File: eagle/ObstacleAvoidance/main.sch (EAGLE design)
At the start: 19 parts, among them IC1 L293D, X1 JST-XH-02-PIN-LONG-PAD, X2 JST-XH-02-PIN-LONG-PAD, X3 JST-XH-04-PIN-LONG-PAD

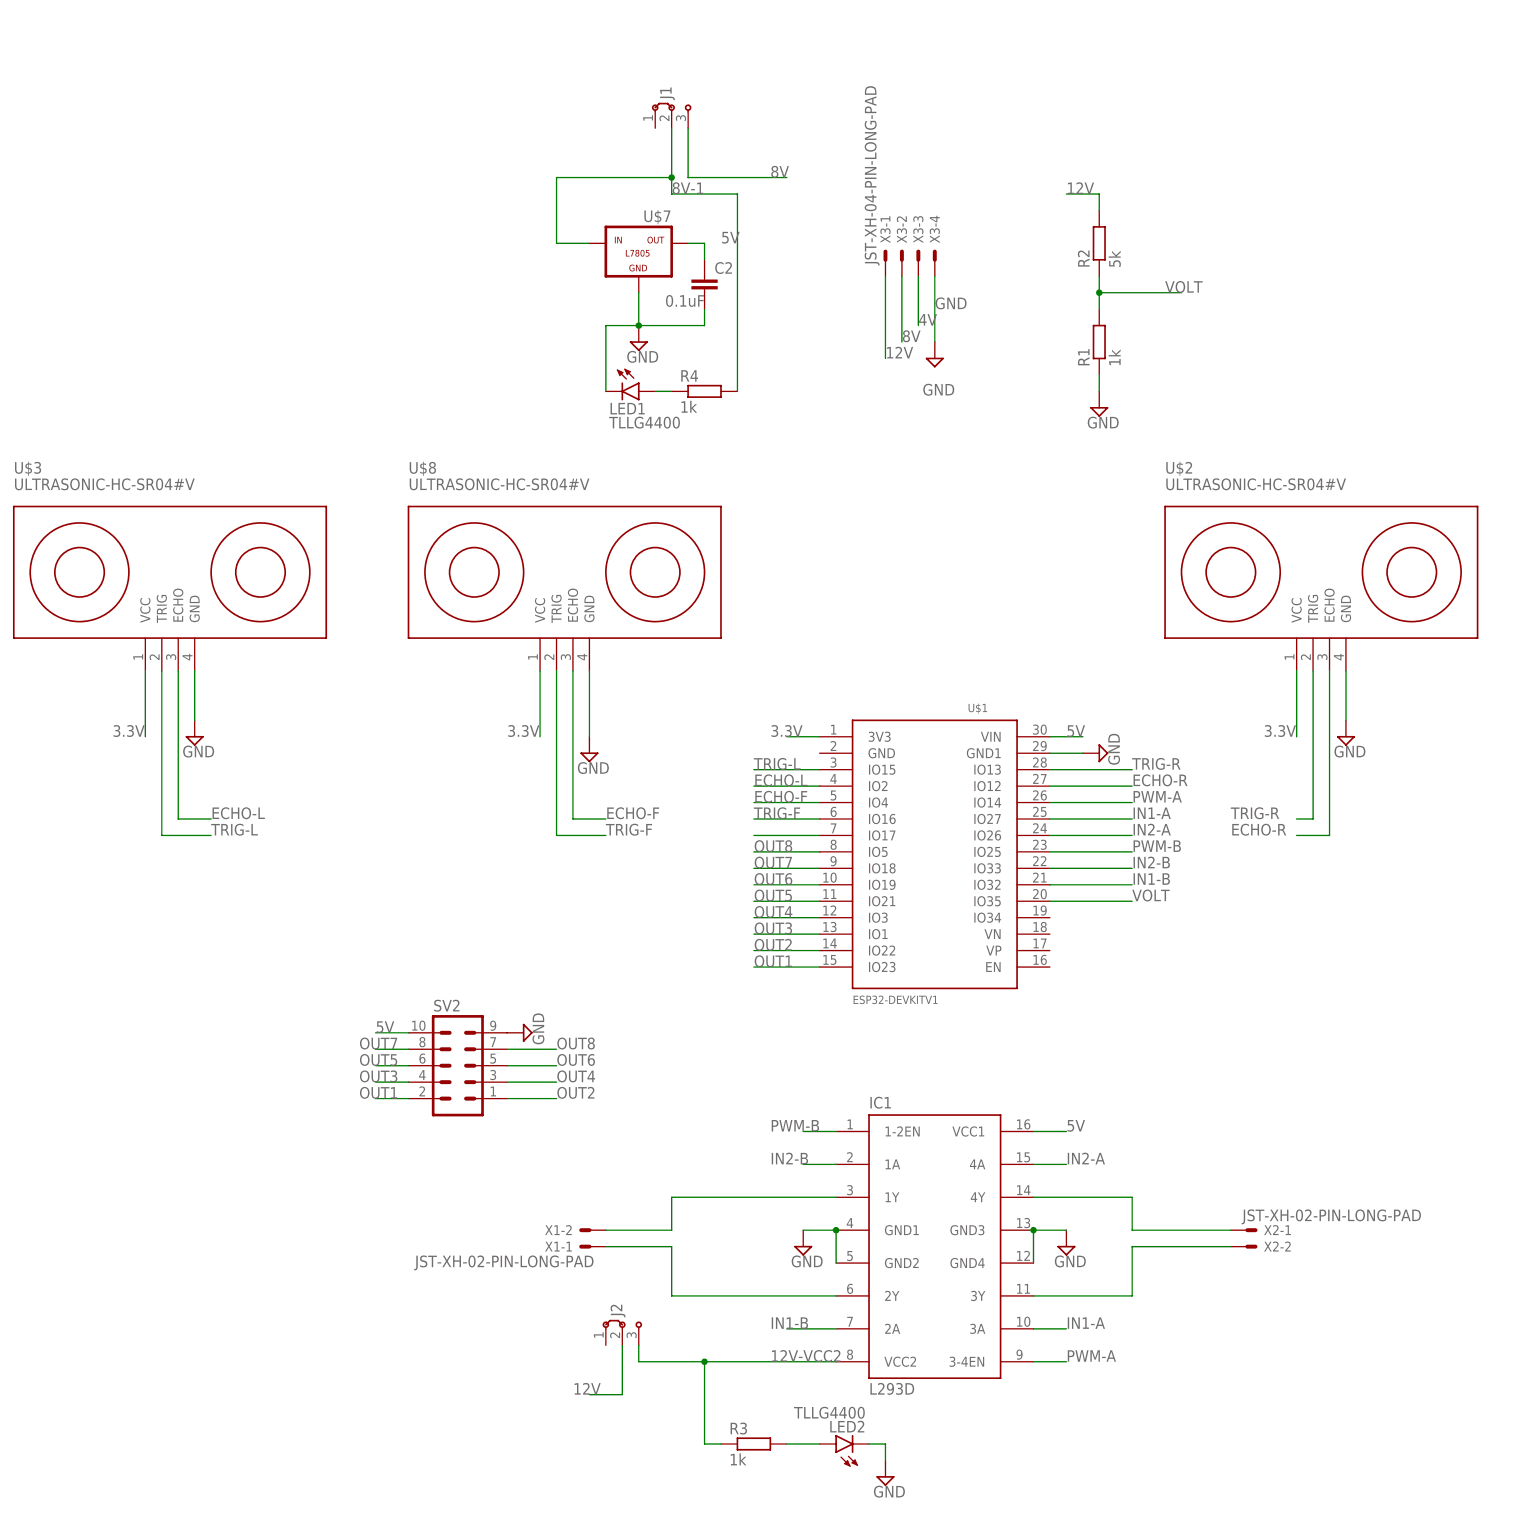
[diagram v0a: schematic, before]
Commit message: Feat: New PCB routing
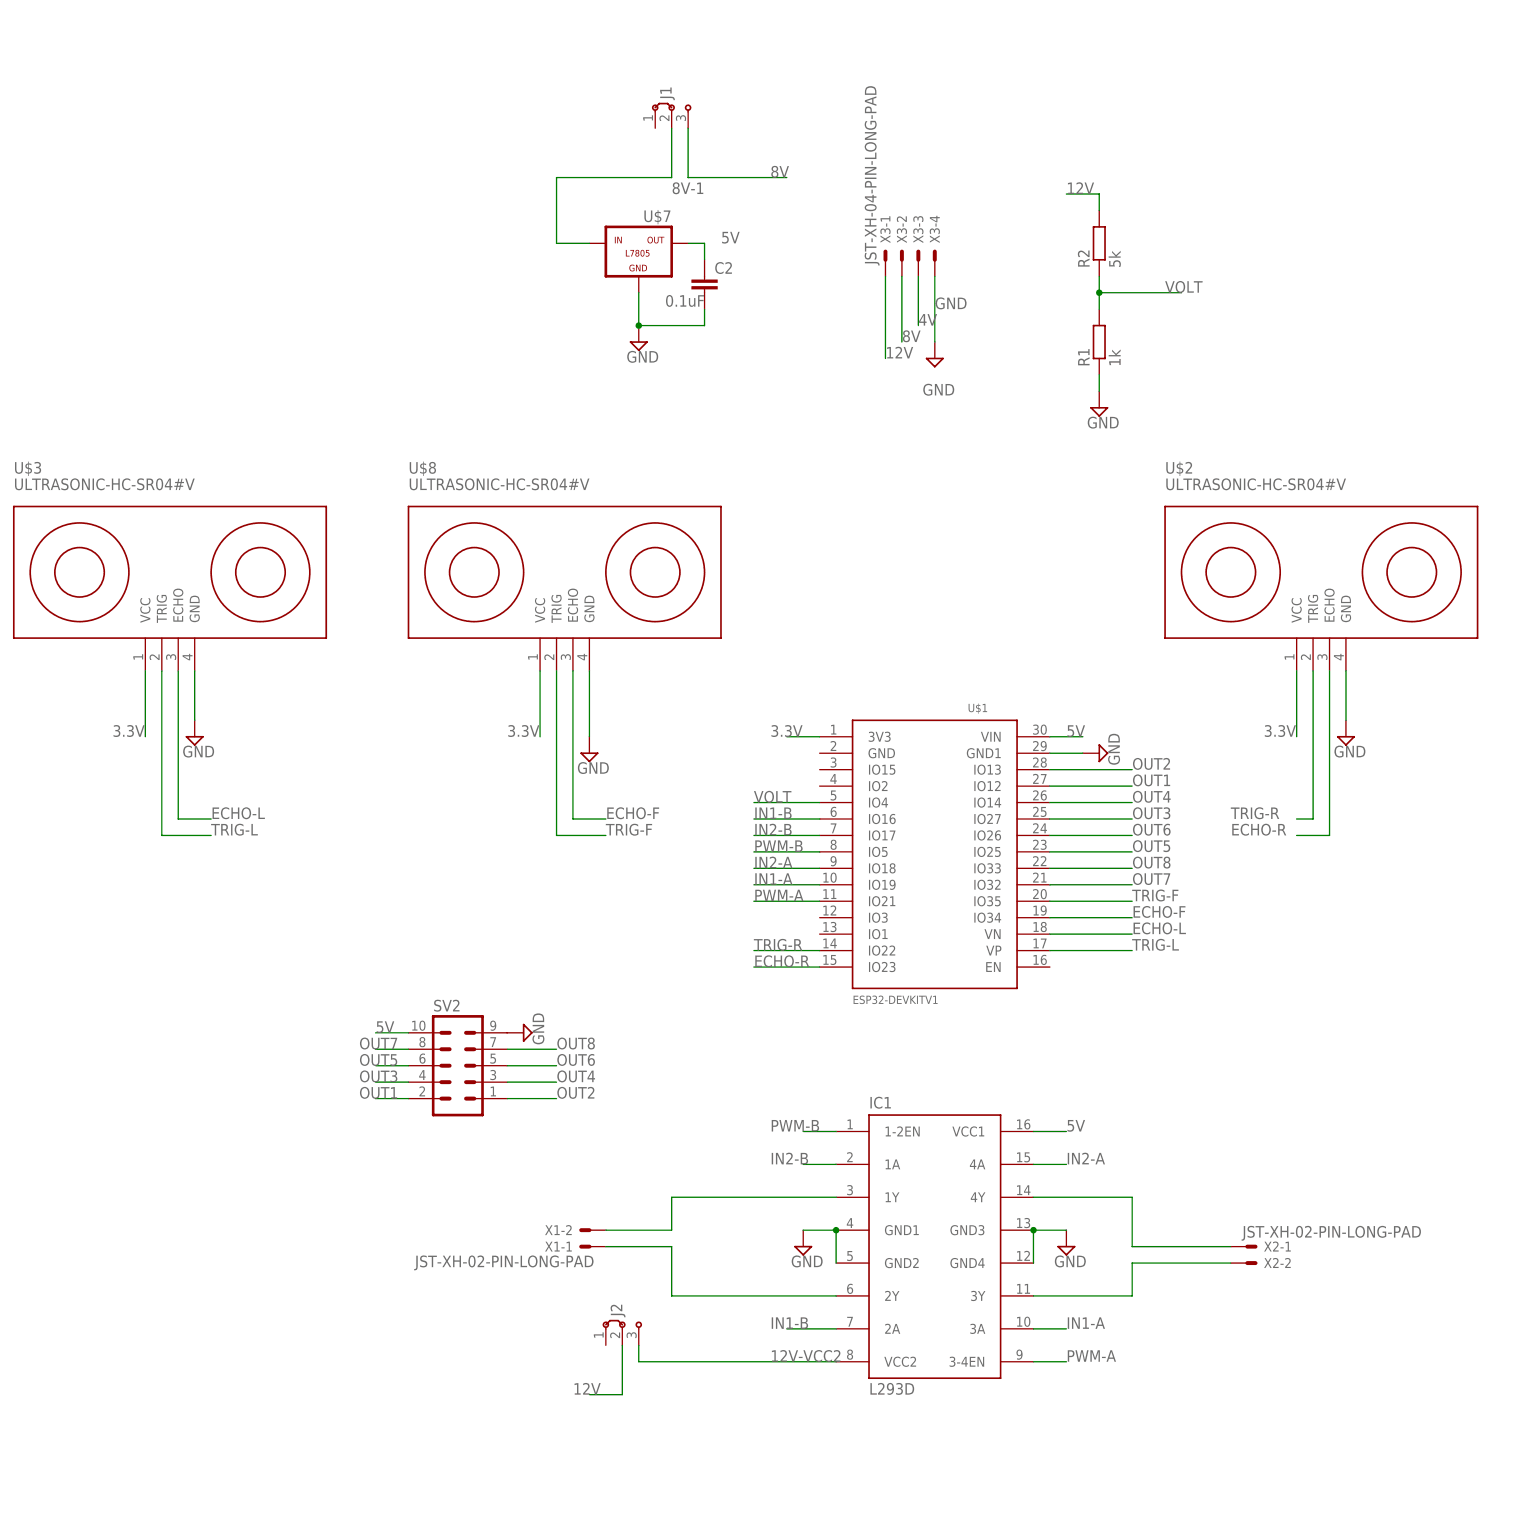
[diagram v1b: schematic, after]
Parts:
- removed LED1, LED2: TLLG4400, led:TLLG4400
- removed R3, R4: 1k, rcl:R-EU_0207/10
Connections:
- removed net N$15: U$1.IO17
- removed net N$5: LED1.A, R4.1
- removed net N$9: LED2.A, R3.2
- net 12V-VCC2: no longer R3.1
- net 8V-1: no longer R4.2
- net ECHO-F: now also U$1.IO34; no longer U$1.IO4
- net ECHO-L: now also U$1.VN; no longer U$1.IO2
- net ECHO-R: now also U$1.IO23; no longer U$1.IO12
- net GND: no longer LED1.C, LED2.C
- net IN1-A: now also U$1.IO19; no longer U$1.IO27
- net IN1-B: now also U$1.IO16; no longer U$1.IO32
- net IN2-A: now also U$1.IO18; no longer U$1.IO26
- net IN2-B: now also U$1.IO17; no longer U$1.IO33
- net OUT1: now also U$1.IO12; no longer U$1.IO23
- net OUT2: now also U$1.IO13; no longer U$1.IO22
- net OUT3: now also U$1.IO27; no longer U$1.IO1
- net OUT4: now also U$1.IO14; no longer U$1.IO3
- net OUT5: now also U$1.IO25; no longer U$1.IO21
- net OUT6: now also U$1.IO26; no longer U$1.IO19
- net OUT7: now also U$1.IO32; no longer U$1.IO18
- net OUT8: now also U$1.IO33; no longer U$1.IO5
- net PWM-A: now also U$1.IO21; no longer U$1.IO14
- net PWM-B: now also U$1.IO5; no longer U$1.IO25
- net TRIG-F: now also U$1.IO35; no longer U$1.IO16
- net TRIG-L: now also U$1.VP; no longer U$1.IO15
- net TRIG-R: now also U$1.IO22; no longer U$1.IO13
- net VOLT: now also U$1.IO4; no longer U$1.IO35
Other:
- moved on the sheet: X2-1, X2-2

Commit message: Feat: Deleted buttons
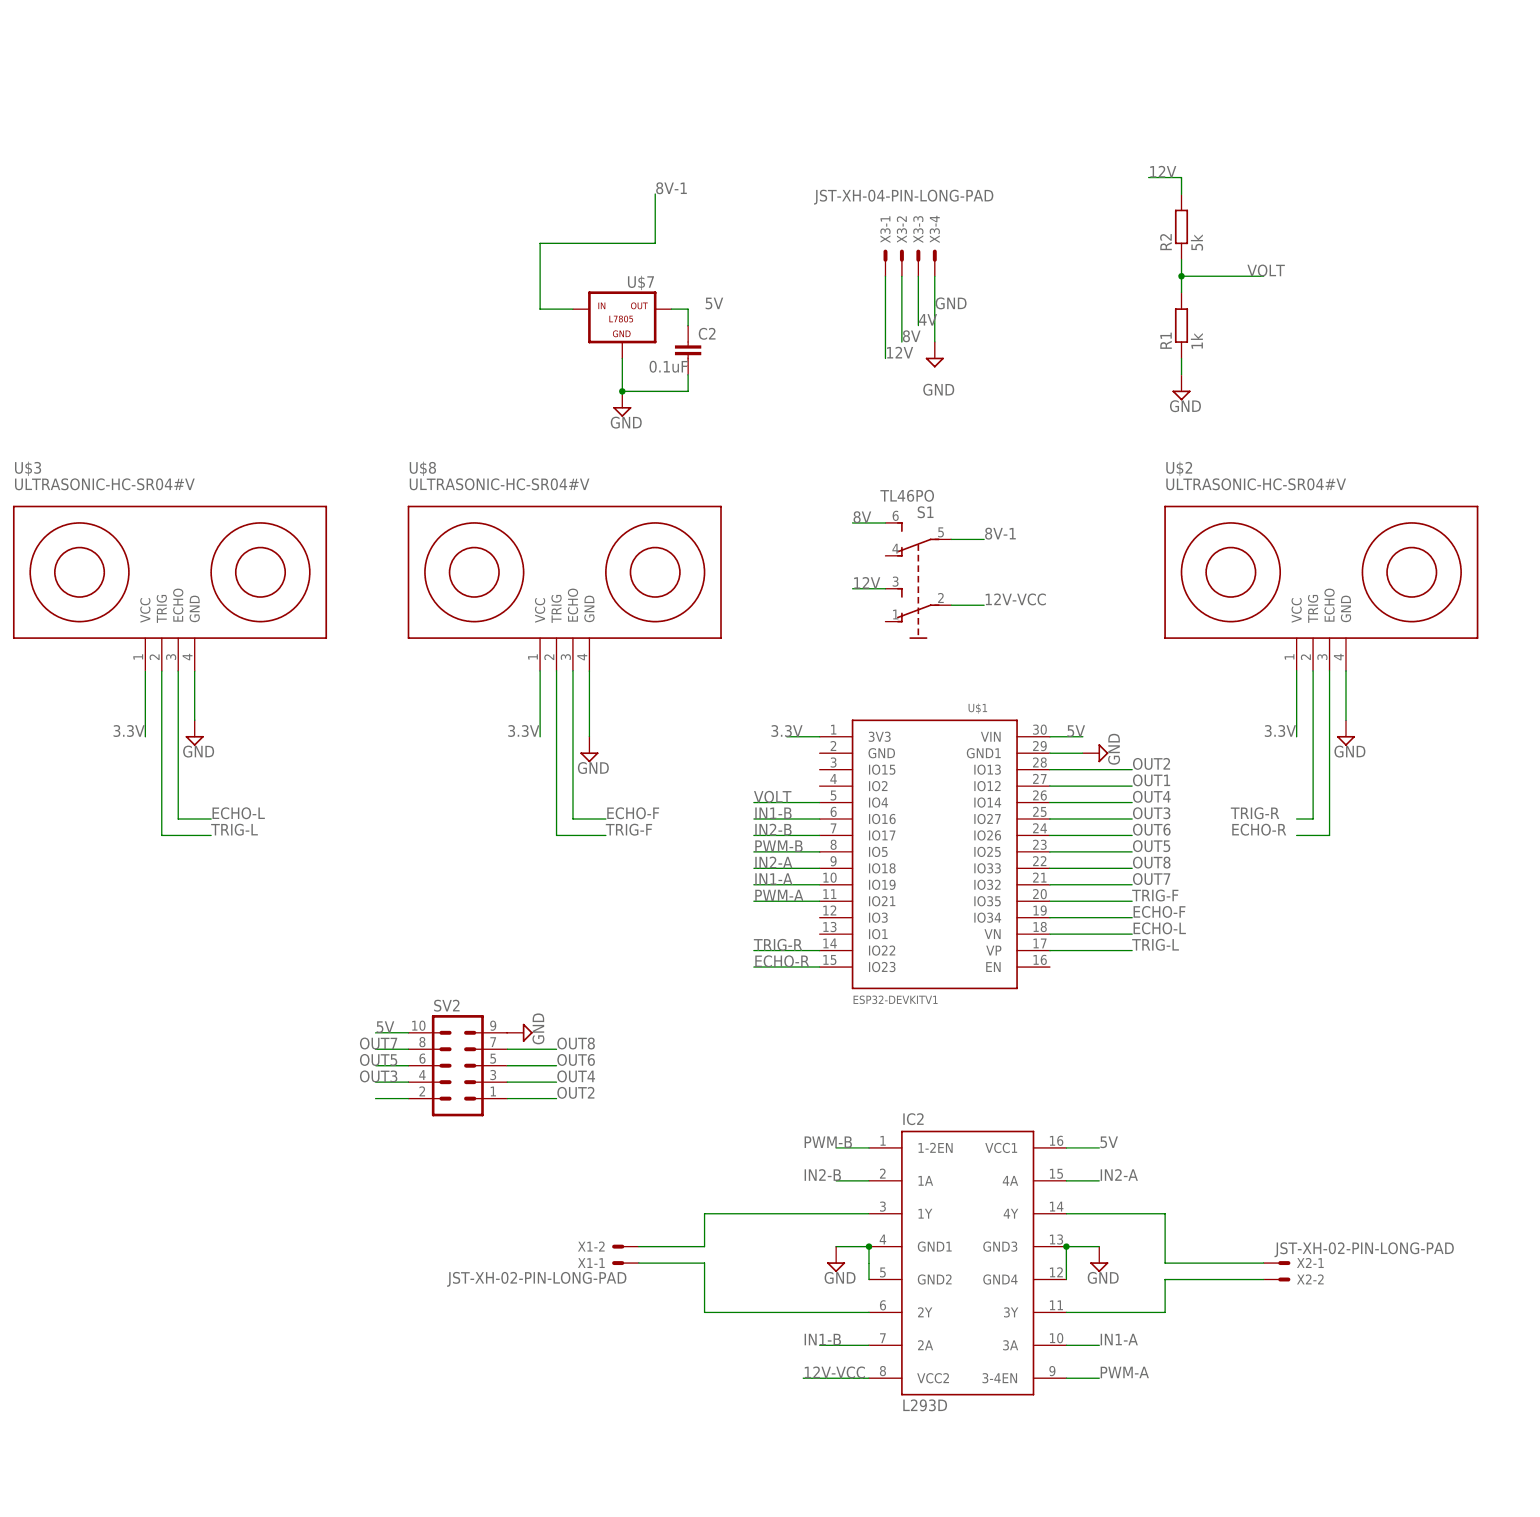
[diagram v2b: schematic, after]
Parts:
- removed IC1: L293D, st-microelectronics:L293D
- removed J1, J2: (no value), jumper:J2X5MM
- added IC2: L293D, st-microelectronics:L293D
- added S1: TL46PO, switch:TL46PO
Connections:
- removed net 12V-VCC2: IC1.VCC2, J2.3
- new net 12V-VCC: IC2.VCC2, S1.P
- new net N$5: IC2.GND2
- new net N$6: IC2.GND4
- new net OUT9: SV2.2
- net 12V: now also S1.S; no longer J2.2
- net 5V: now also IC2.VCC1; no longer IC1.VCC1
- net 8V: now also S1.S1; no longer J1.3
- net 8V-1: now also S1.P1; no longer J1.2
- net GND: now also IC2.GND1, IC2.GND3; no longer IC1.GND1, IC1.GND2, IC1.GND3, IC1.GND4
- net IN1-A: now also IC2.3A; no longer IC1.3A
- net IN1-B: now also IC2.2A; no longer IC1.2A
- net IN2-A: now also IC2.4A; no longer IC1.4A
- net IN2-B: now also IC2.1A; no longer IC1.1A
- net N$1: now also IC2.1Y; no longer IC1.1Y
- net N$2: now also IC2.2Y; no longer IC1.2Y
- net N$3: now also IC2.4Y; no longer IC1.4Y
- net N$4: now also IC2.3Y; no longer IC1.3Y
- net OUT1: no longer SV2.2
- net PWM-A: now also IC2.3-4EN; no longer IC1.3-4EN
- net PWM-B: now also IC2.1-2EN; no longer IC1.1-2EN
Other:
- moved on the sheet: C2, R1, R2, U$7, X1-1, X1-2, X2-1, X2-2
